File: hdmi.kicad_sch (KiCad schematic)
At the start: 47 parts, among them Q3 NVJD4401NT1G, U15 TPD4E05U06QDQARQ1, U17 TPD4E05U06QDQARQ1, U18 TPD4E05U06QDQARQ1, U21 SN75DP159_VQFN, U22 SN74AVC2T245_UQFN, U23 NTS0104BQ, U24 SN74LVC1T45_SOT-5X3

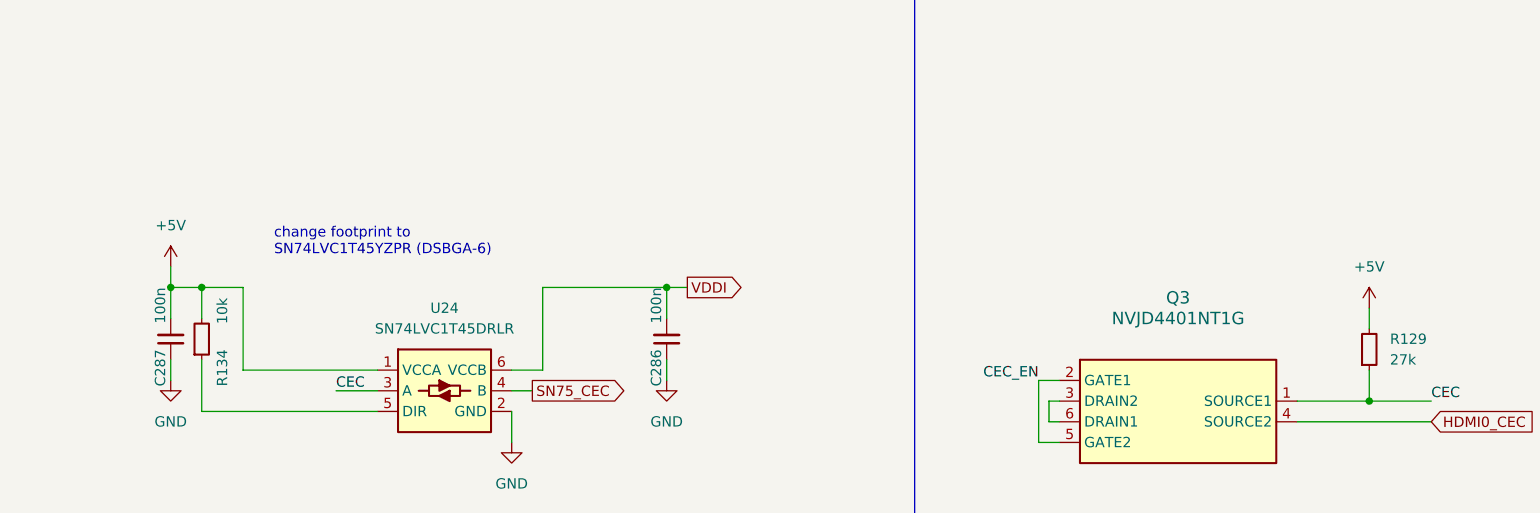
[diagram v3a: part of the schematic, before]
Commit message: [#53847] Pull-up CEC to 3V3
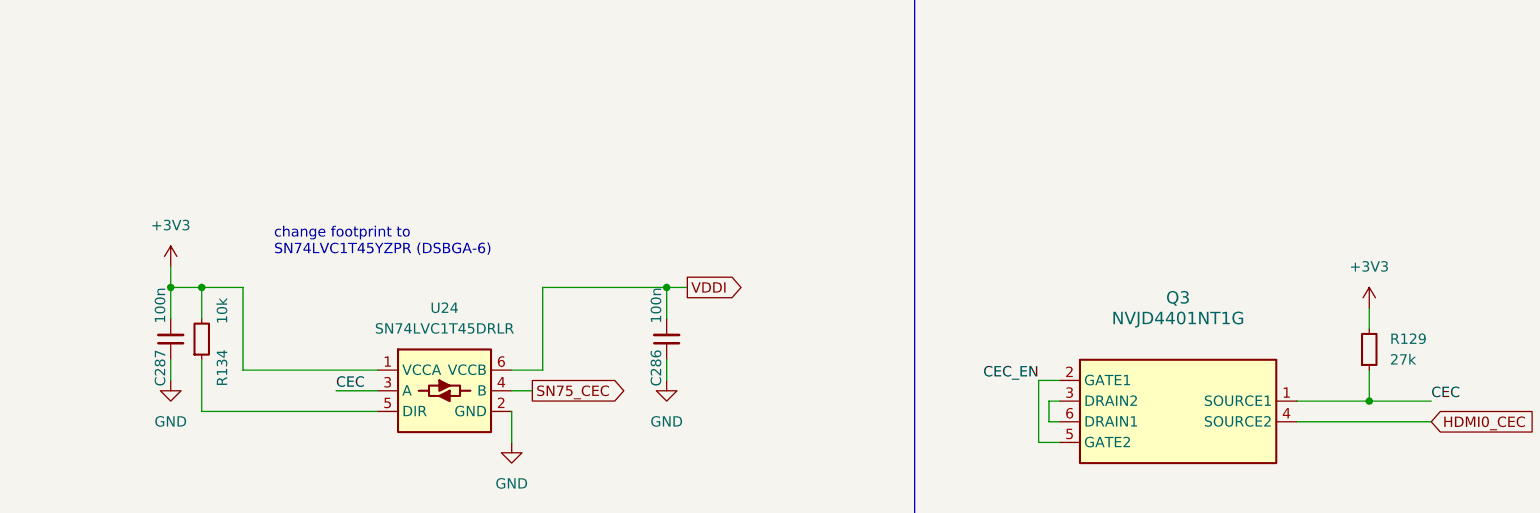
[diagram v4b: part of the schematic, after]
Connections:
- net +3V3: now also C287.2, R129.2, R134.2, U24.1 (VCCA)
- net +5V: no longer C287.2, R129.2, R134.2, U24.1 (VCCA)
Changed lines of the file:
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@@
-    )
-  )
-  (symbol (lib_id "antmicropower:+5V") (at 378.46 66.04 0) (unit 1)
-    (in_bom yes) (on_board yes) (dnp no) (fields_autoplaced)
-    (property "Reference" "#PWR034" (at 393.7 68.58 0)
-      (effects (font (size 1.27 1.27) (thickness 0.15)) (justify left bottom) hide)
-    )
-    (property "Value" "+5V" (at 378.46 60.96 0)
-      (effects (font (size 1.27 1.27) (thickness 0.15)))
-    )
-    (property "Footprint" "" (at 393.7 73.66 0)
-      (effects (font (size 1.27 1.27) (thickness 0.15)) (justify left bottom) hide)
-    )
-    (property "Datasheet" "" (at 393.7 76.2 0)
-      (effects (font (size 1.27 1.27) (thickness 0.15)) (justify left bottom) hide)
-    )
-    (property "Author" "Antmicro" (at 393.7 73.66 0)
-      (effects (font (size 1.27 1.27) (thickness 0.15)) (justify left bottom) hide)
-    )
-    (property "License" "Apache-2.0" (at 393.7 76.2 0)
-      (effects (font (size 1.27 1.27) (thickness 0.15)) (justify left bottom) hide)
-    )
-    (pin "1")
-    (instances
-      (project "polarfire-som"
-        (path "/db4a0d3e-2eb3-499e-977d-6eb378cfd3ed/9d03ca8b-00f4-4bc6-89d1-f3be2c1a83b3"
-          (reference "#PWR034") (unit 1)
-        )
-      )
     )
   )
@@
     )
   )
+  (symbol (lib_id "antmicropower:+3V3") (at 378.46 66.04 0) (unit 1)
+    (in_bom yes) (on_board yes) (dnp no) (fields_autoplaced)
+    (property "Reference" "#PWR053" (at 393.7 66.04 0)
+      (effects (font (size 1.27 1.27) (thickness 0.15)) (justify left bottom) hide)
+    )
+    (property "Value" "+3V3" (at 378.46 60.96 0)
+      (effects (font (size 1.27 1.27) (thickness 0.15)))
+    )
+    (property "Footprint" "" (at 393.7 73.66 0)
+      (effects (font (size 1.27 1.27) (thickness 0.15)) (justify left bottom) hide)
+    )
+    (property "Datasheet" "" (at 393.7 76.2 0)
+      (effects (font (size 1.27 1.27) (thickness 0.15)) (justify left bottom) hide)
+    )
+    (property "Author" "Antmicro" (at 393.7 68.58 0)
+      (effects (font (size 1.27 1.27) (thickness 0.15)) (justify left bottom) hide)
+    )
+    (property "License" "Apache-2.0" (at 393.7 71.12 0)
+      (effects (font (size 1.27 1.27) (thickness 0.15)) (justify left bottom) hide)
+    )
+    (pin "1")
+    (instances
+      (project "polarfire-som"
+        (path "/db4a0d3e-2eb3-499e-977d-6eb378cfd3ed/9d03ca8b-00f4-4bc6-89d1-f3be2c1a83b3"
+          (reference "#PWR053") (unit 1)
+        )
+      )
+    )
+  )
   (symbol (lib_id "antmicroCapacitorsmisc:C_100n_0201") (at 189.23 173.99 0) (unit 1)
     (in_bom yes) (on_board yes) (dnp no)
@@
         (path "/db4a0d3e-2eb3-499e-977d-6eb378cfd3ed/9d03ca8b-00f4-4bc6-89d1-f3be2c1a83b3"
           (reference "C268") (unit 1)
-        )
-      )
-    )
-  )
-  (symbol (lib_id "antmicropower:+5V") (at 231.14 60.96 0) (unit 1)
-    (in_bom yes) (on_board yes) (dnp no) (fields_autoplaced)
-    (property "Reference" "#PWR038" (at 246.38 63.5 0)
-      (effects (font (size 1.27 1.27) (thickness 0.15)) (justify left bottom) hide)
-    )
-    (property "Value" "+5V" (at 231.14 55.88 0)
-      (effects (font (size 1.27 1.27) (thickness 0.15)))
-    )
-    (property "Footprint" "" (at 246.38 68.58 0)
-      (effects (font (size 1.27 1.27) (thickness 0.15)) (justify left bottom) hide)
-    )
-    (property "Datasheet" "" (at 246.38 71.12 0)
-      (effects (font (size 1.27 1.27) (thickness 0.15)) (justify left bottom) hide)
-    )
-    (property "Author" "Antmicro" (at 246.38 68.58 0)
-      (effects (font (size 1.27 1.27) (thickness 0.15)) (justify left bottom) hide)
-    )
-    (property "License" "Apache-2.0" (at 246.38 71.12 0)
-      (effects (font (size 1.27 1.27) (thickness 0.15)) (justify left bottom) hide)
-    )
-    (pin "1")
-    (instances
-      (project "polarfire-som"
-        (path "/db4a0d3e-2eb3-499e-977d-6eb378cfd3ed/9d03ca8b-00f4-4bc6-89d1-f3be2c1a83b3"
-          (reference "#PWR038") (unit 1)
         )
       )
@@
         )
       )
+    )
+  )
+  (symbol (lib_id "antmicropower:+3V3") (at 231.14 60.96 0) (unit 1)
+    (in_bom yes) (on_board yes) (dnp no) (fields_autoplaced)
+    (property "Reference" "#PWR054" (at 246.38 60.96 0)
+      (effects (font (size 1.27 1.27) (thickness 0.15)) (justify left bottom) hide)
+    )
+    (property "Value" "+3V3" (at 231.14 55.88 0)
+      (effects (font (size 1.27 1.27) (thickness 0.15)))
+    )
+    (property "Footprint" "" (at 246.38 68.58 0)
+      (effects (font (size 1.27 1.27) (thickness 0.15)) (justify left bottom) hide)
+    )
+    (property "Datasheet" "" (at 246.38 71.12 0)
+      (effects (font (size 1.27 1.27) (thickness 0.15)) (justify left bottom) hide)
+    )
+    (property "Author" "Antmicro" (at 246.38 63.5 0)
+      (effects (font (size 1.27 1.27) (thickness 0.15)) (justify left bottom) hide)
+    )
+    (property "License" "Apache-2.0" (at 246.38 66.04 0)
+      (effects (font (size 1.27 1.27) (thickness 0.15)) (justify left bottom) hide)
+    )
+    (pin "1")
+    (instances
+      (project "polarfire-som"
+        (path "/db4a0d3e-2eb3-499e-977d-6eb378cfd3ed/9d03ca8b-00f4-4bc6-89d1-f3be2c1a83b3"
+          (reference "#PWR054") (unit 1)
+        )
+      )

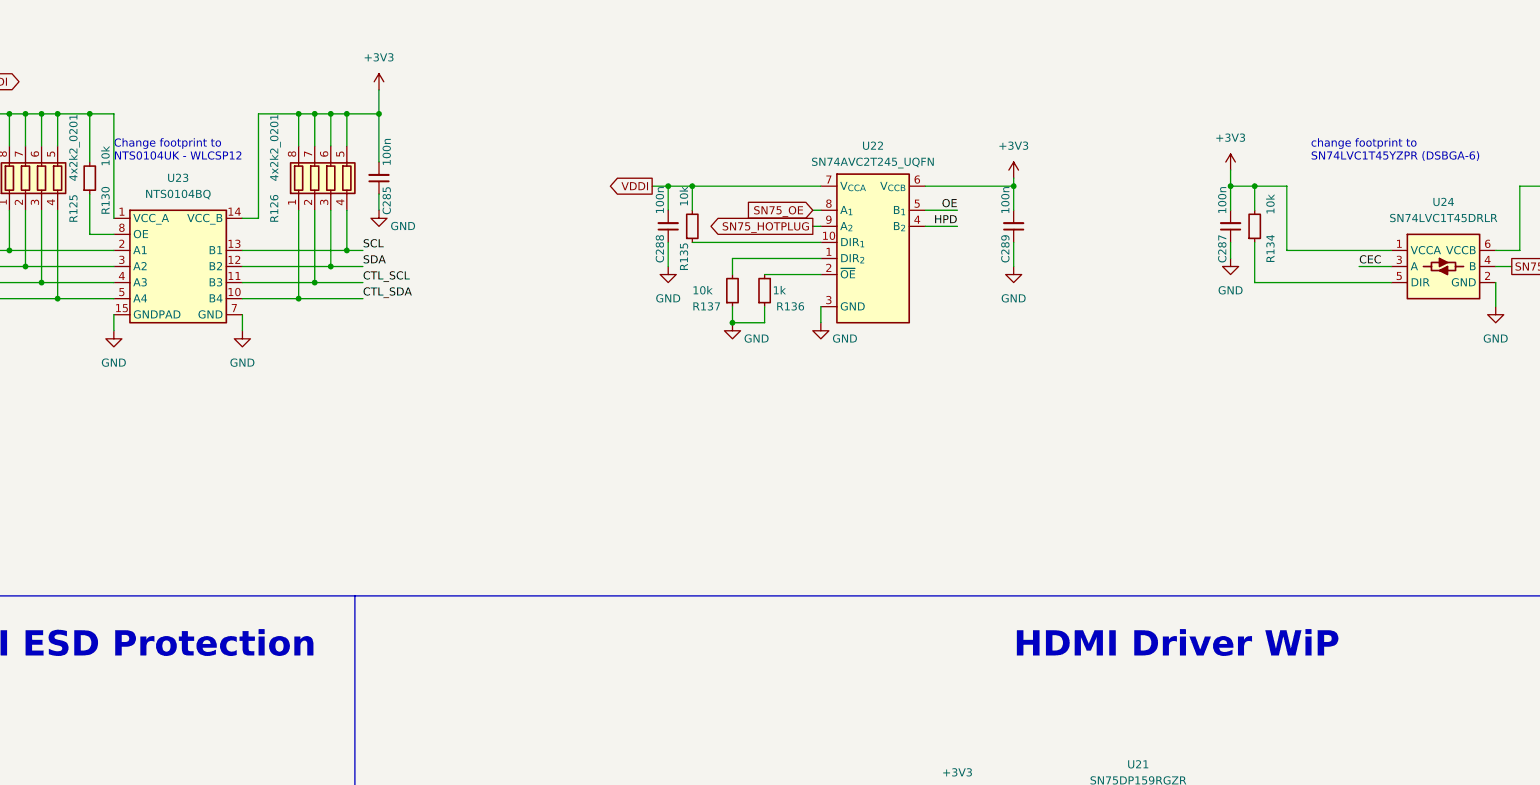
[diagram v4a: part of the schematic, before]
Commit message: [#53847] Change NTS0104BQ to NTS0104UK
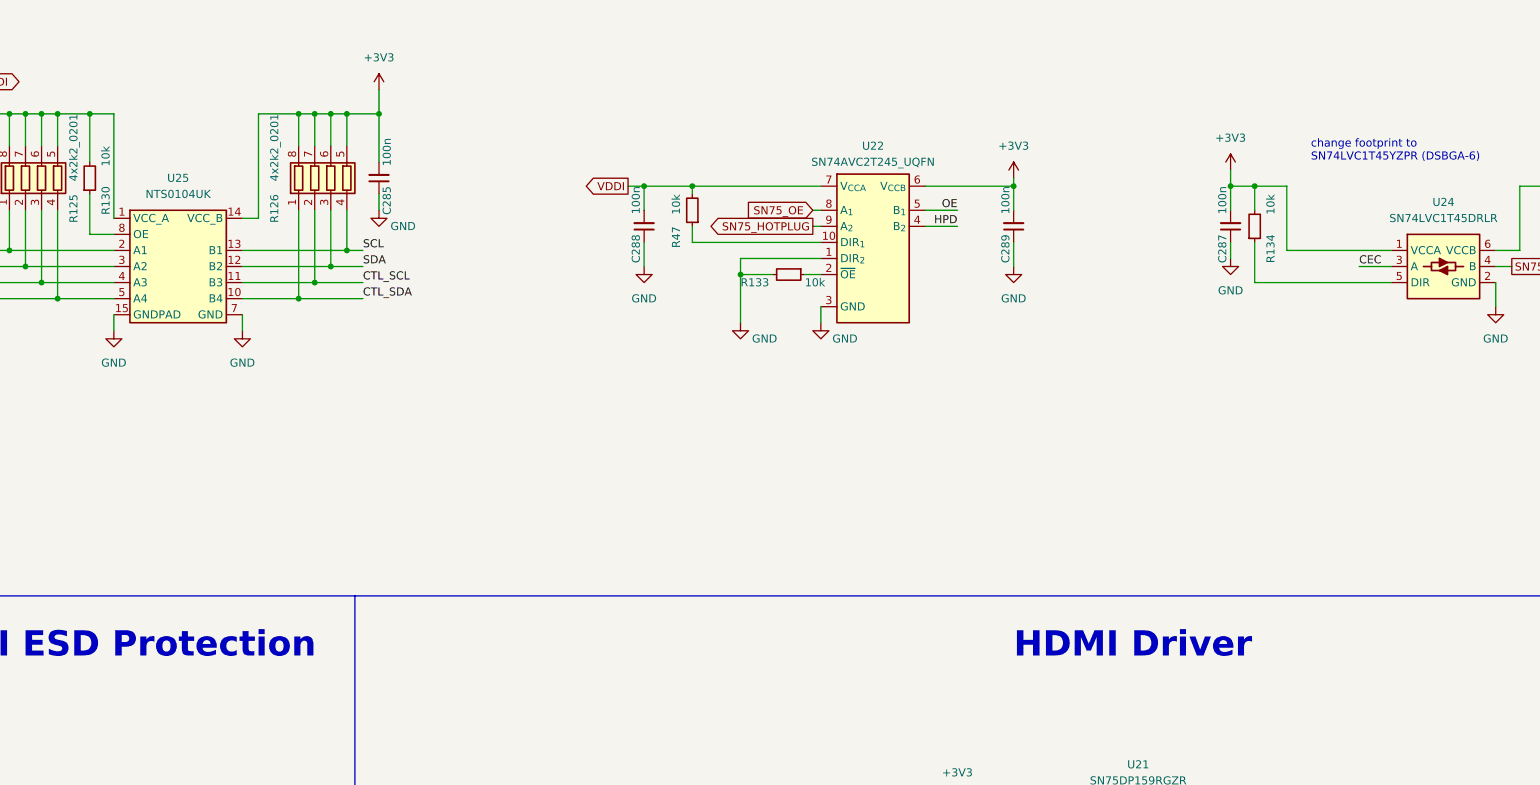
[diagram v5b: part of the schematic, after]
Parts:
- removed R135, R137: R_10k_0402, antmicro-footprints:R_0402_1005Metric, symbol antmicroResistors0402:R_10k_0402
- removed R136: R_1k_0402, antmicro-footprints:R_0402_1005Metric, symbol antmicroResistors0402:R_1k_0402
- removed U23: NTS0104BQ, antmicro-footprints:DHVQFN-14-1EP_2.5x3mm, symbol antmicroLogicTranslatorsLevelShifters:NTS0104BQ
- added R133, R47: R_10k_0402, antmicro-footprints:R_0402_1005Metric, symbol antmicroResistors0402:R_10k_0402
- added U25: NTS0104UK, antmicro-footprints:WLCSP-12_1.2x1.6mm, symbol antmicroLogicTranslatorsLevelShifters:NTS0104UK
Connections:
- net +3V3: now also U25.14 (VCC_B)
- net CTL_SCL: now also U25.11 (B3)
- net CTL_SDA: now also U25.10 (B4)
- net GND: now also U22.1 (DIR_{2}), R133.2, U25.15 (GNDPAD), U25.7 (GND)
- net SCL: now also U25.13 (B1)
- net SDA: now also U25.12 (B2)
- net SN75_CTL_SCL: now also U25.4 (A3)
- net SN75_CTL_SDA: now also U25.5 (A4)
- net SN75_SCL: now also U25.2 (A1)
- net SN75_SDA: now also U25.3 (A2)
- net VDDI: now also R47.2, U25.1 (VCC_A)
- net at R130.1: now also U25.8 (OE)
- net at U22.10 (DIR_{1}): now also R47.1
- net at U22.2 (~{OE}): now also R133.1
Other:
- note added: "HDMI Driver"
- note removed: "Change footprint to NTS0104UK - WLCSP12"
- note removed: "HDMI Driver WiP"
- moved on the sheet: C288

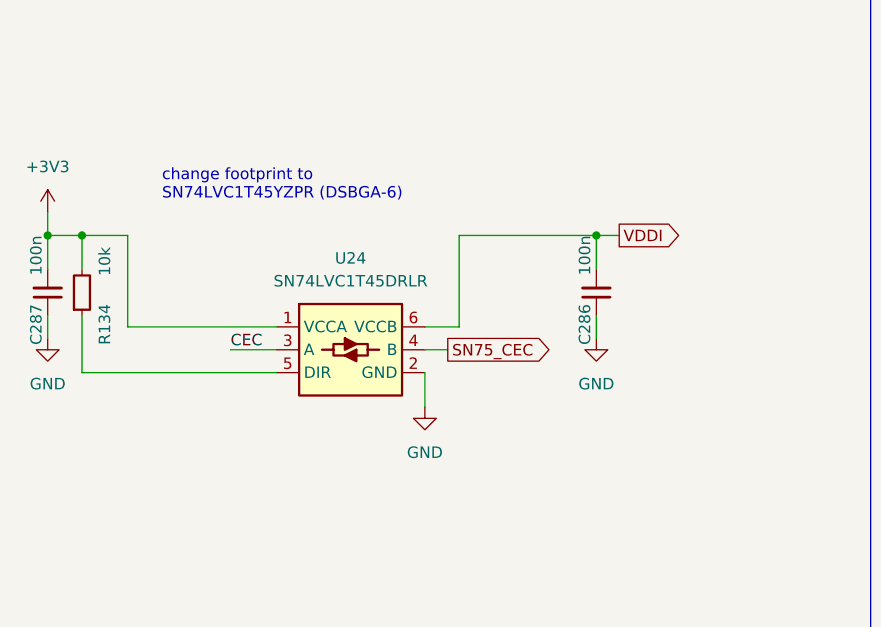
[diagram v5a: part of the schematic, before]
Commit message: [#53847] Replace SN74LVC1T with SN74LVC1T45YZPR
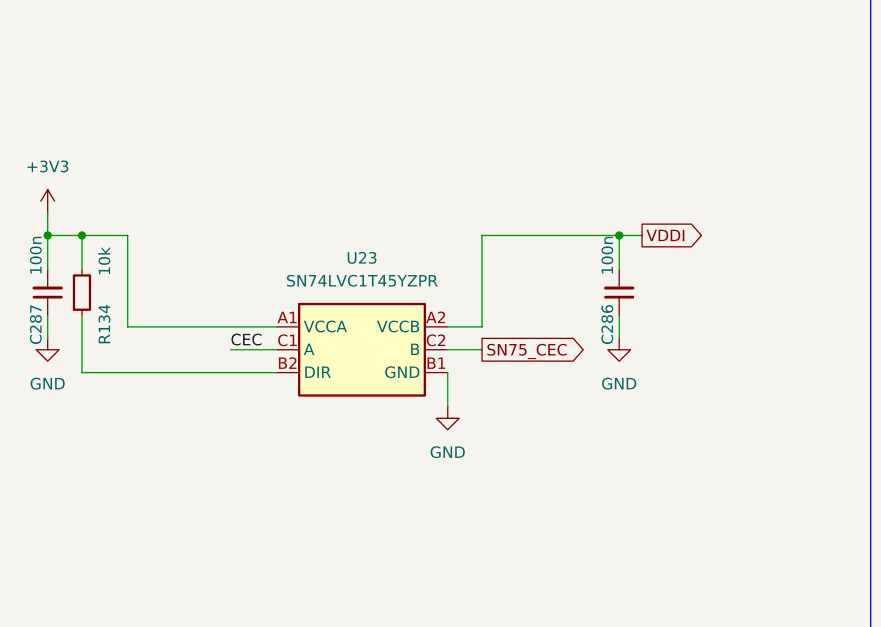
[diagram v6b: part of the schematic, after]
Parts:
- removed U24: SN74LVC1T45_SOT-5X3, antmicro-footprints:SOT-553-6, symbol antmicroLogicTranslatorsLevelShifters:SN74LVC1T45_SOT-5X3
- added U23: SN74LVC1T45YZPR, antmicro-footprints:Texas_DSBGA-6_1.39x0.9mm_Layout2x3_P0.5mm, symbol antmicroLogicTranslatorsLevelShifters:SN74LVC1T45YZPR
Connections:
- net +3V3: now also U23.A1 (VCCA)
- net CEC: now also U23.C1 (A)
- net GND: now also U23.B1 (GND)
- net SN75_CEC: now also U23.C2 (B)
- net VDDI: now also U23.A2 (VCCB)
- net at R134.1: now also U23.B2 (DIR)
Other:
- note removed: "change footprint to SN74LVC1T45YZPR (DSBGA-6)"
- moved on the sheet: C286
